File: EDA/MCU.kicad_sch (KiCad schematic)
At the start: 1 part, among them U7 STM32N657L0H3Q

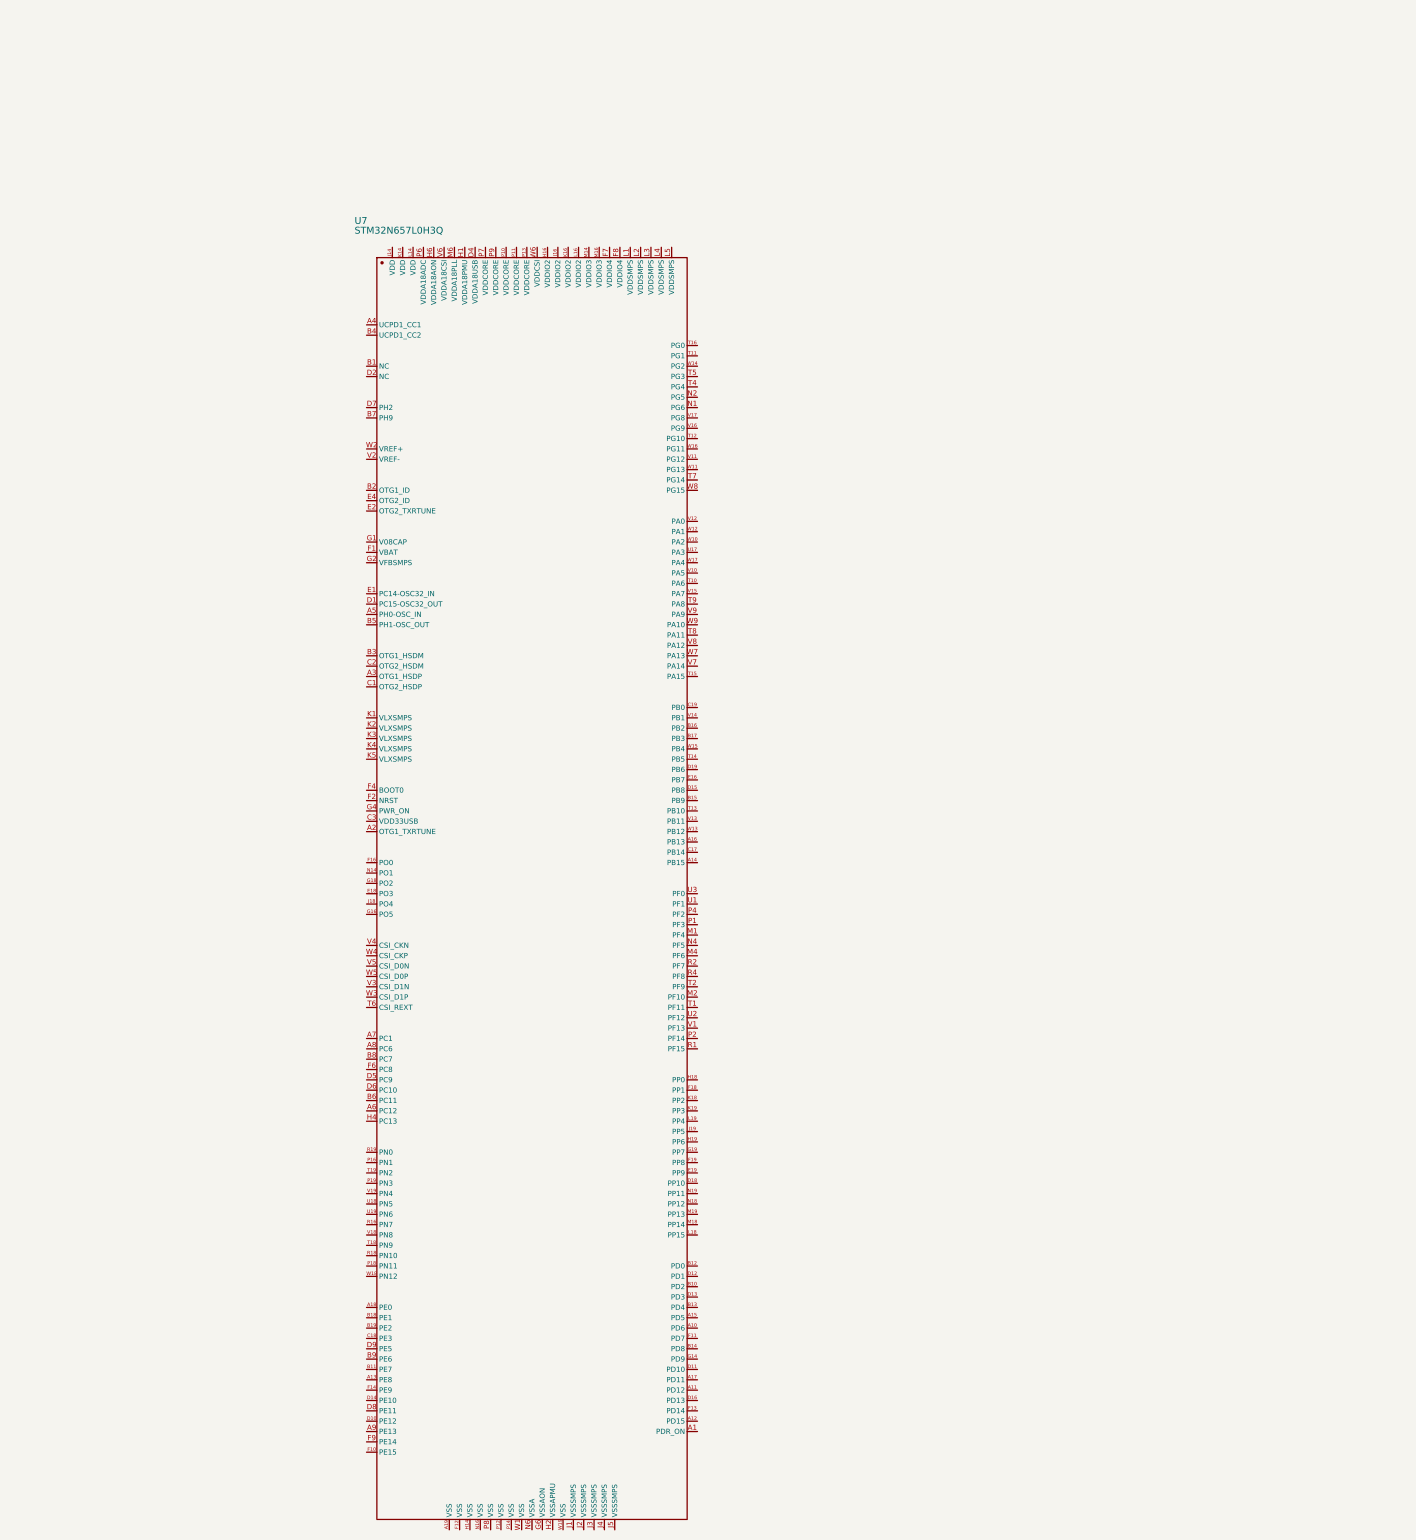
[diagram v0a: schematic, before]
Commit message: Changed STM32 MCU type, and added SDRAM. Micro-SD card slot has also been set up.
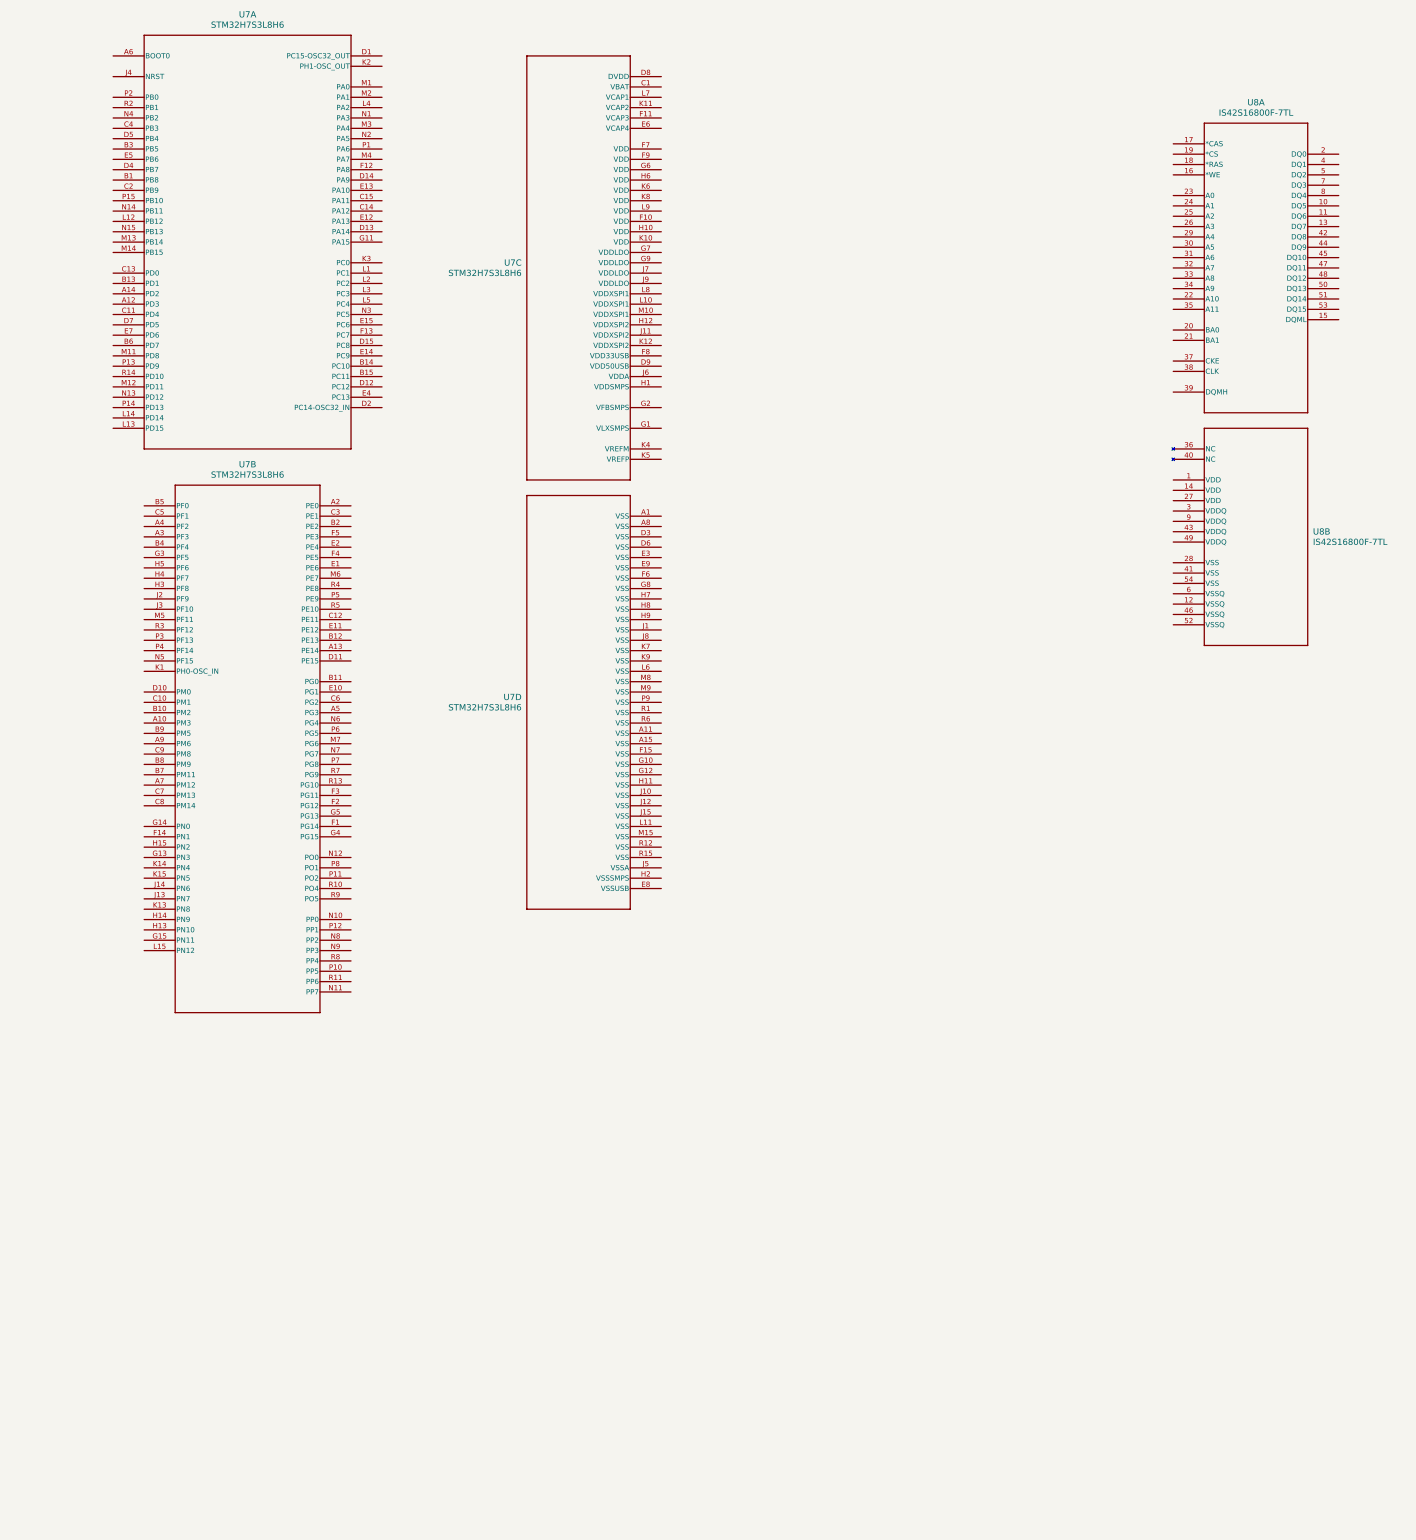
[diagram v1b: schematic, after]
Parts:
- removed U7: STM32N657L0H3Q, symbol STM32N657L0H3Q
- added U7: STM32H7S3L8H6, TFBGA225_13X13_STM, symbol CANSAT-lib:STM32H7S3L8H6
- added U8: IS42S16800F-7TL, CANSAT-lib:TSOP-II-54_ISI, symbol CANSAT-lib:IS42S16800F-7TL

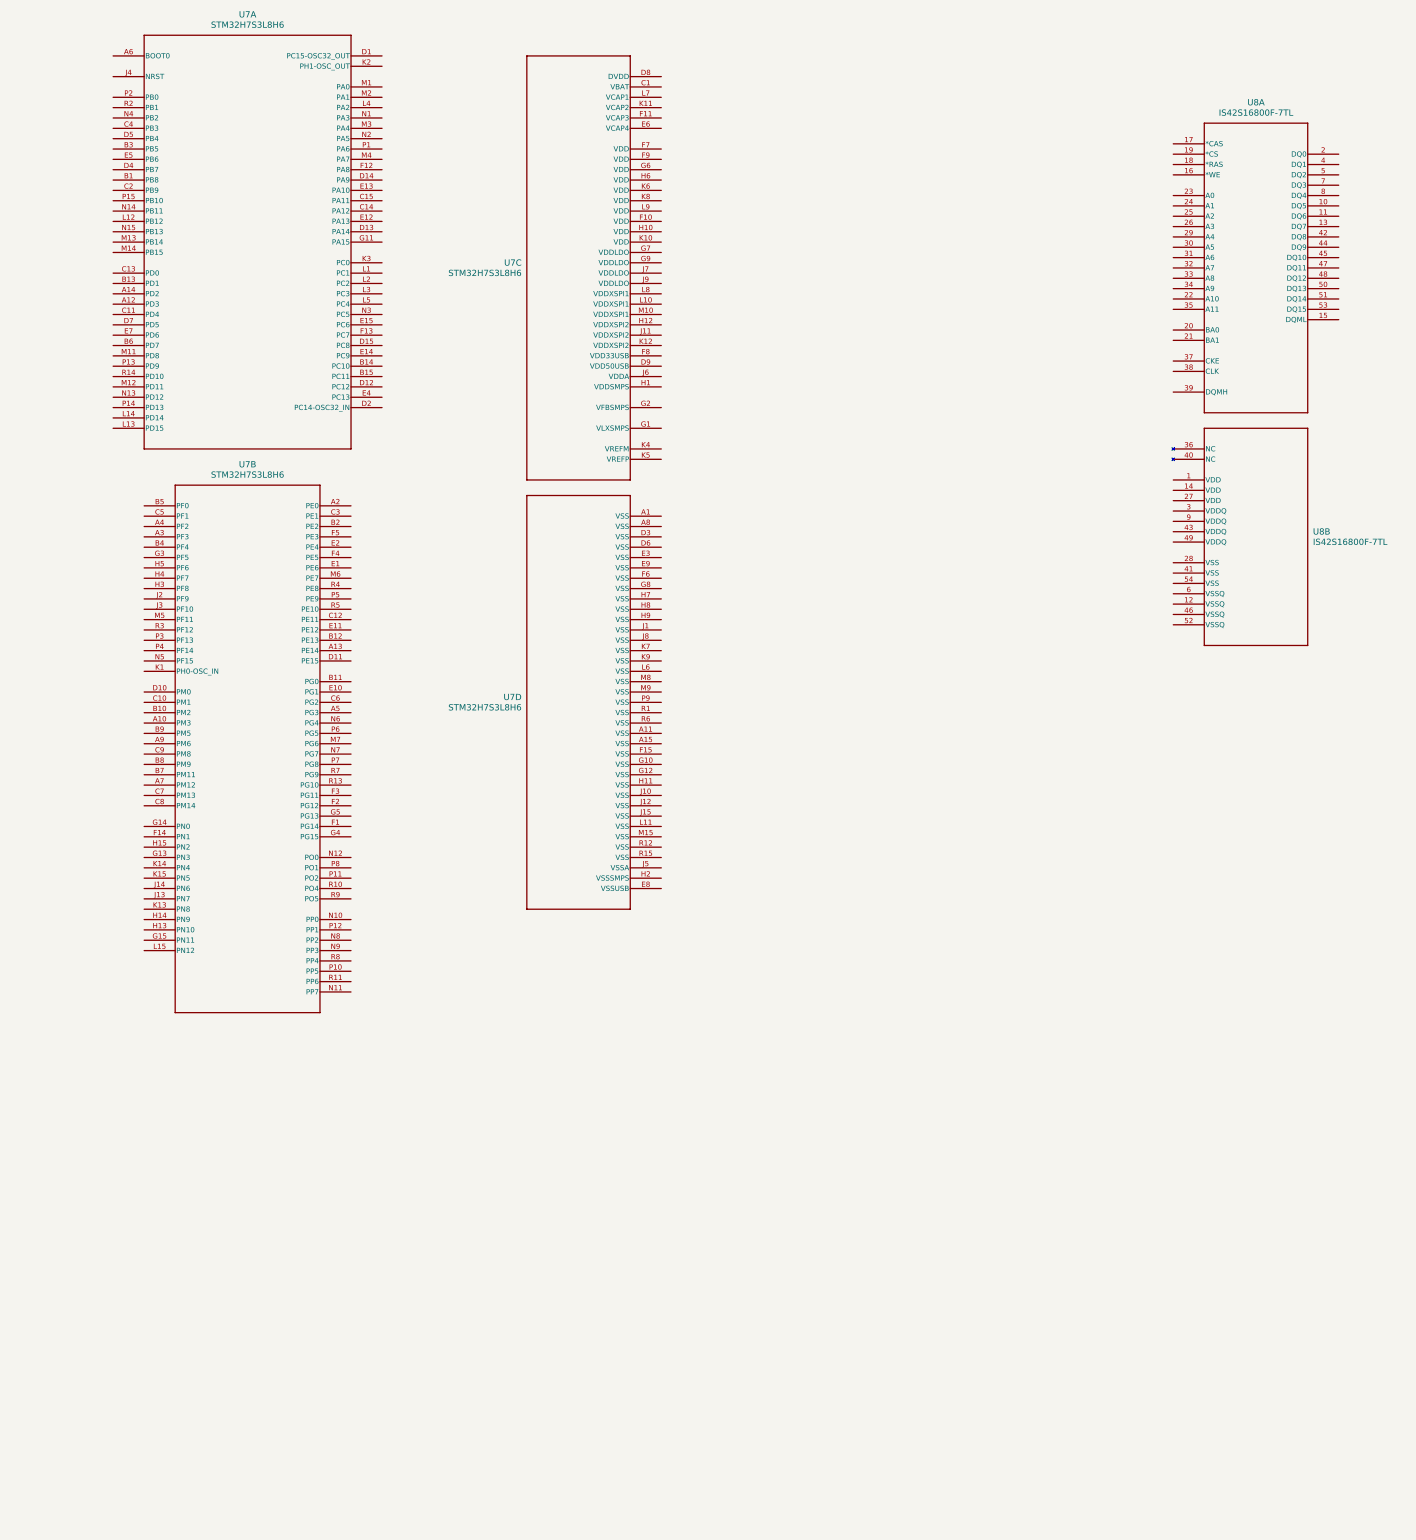
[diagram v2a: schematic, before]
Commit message: Did some scheamtic restruscturing as well as hooked up SDRAM and Micro-SD to STM32 core. Additional low power STM32 has also been added to power control. Firmware .IOC files have also been added for both STM32's
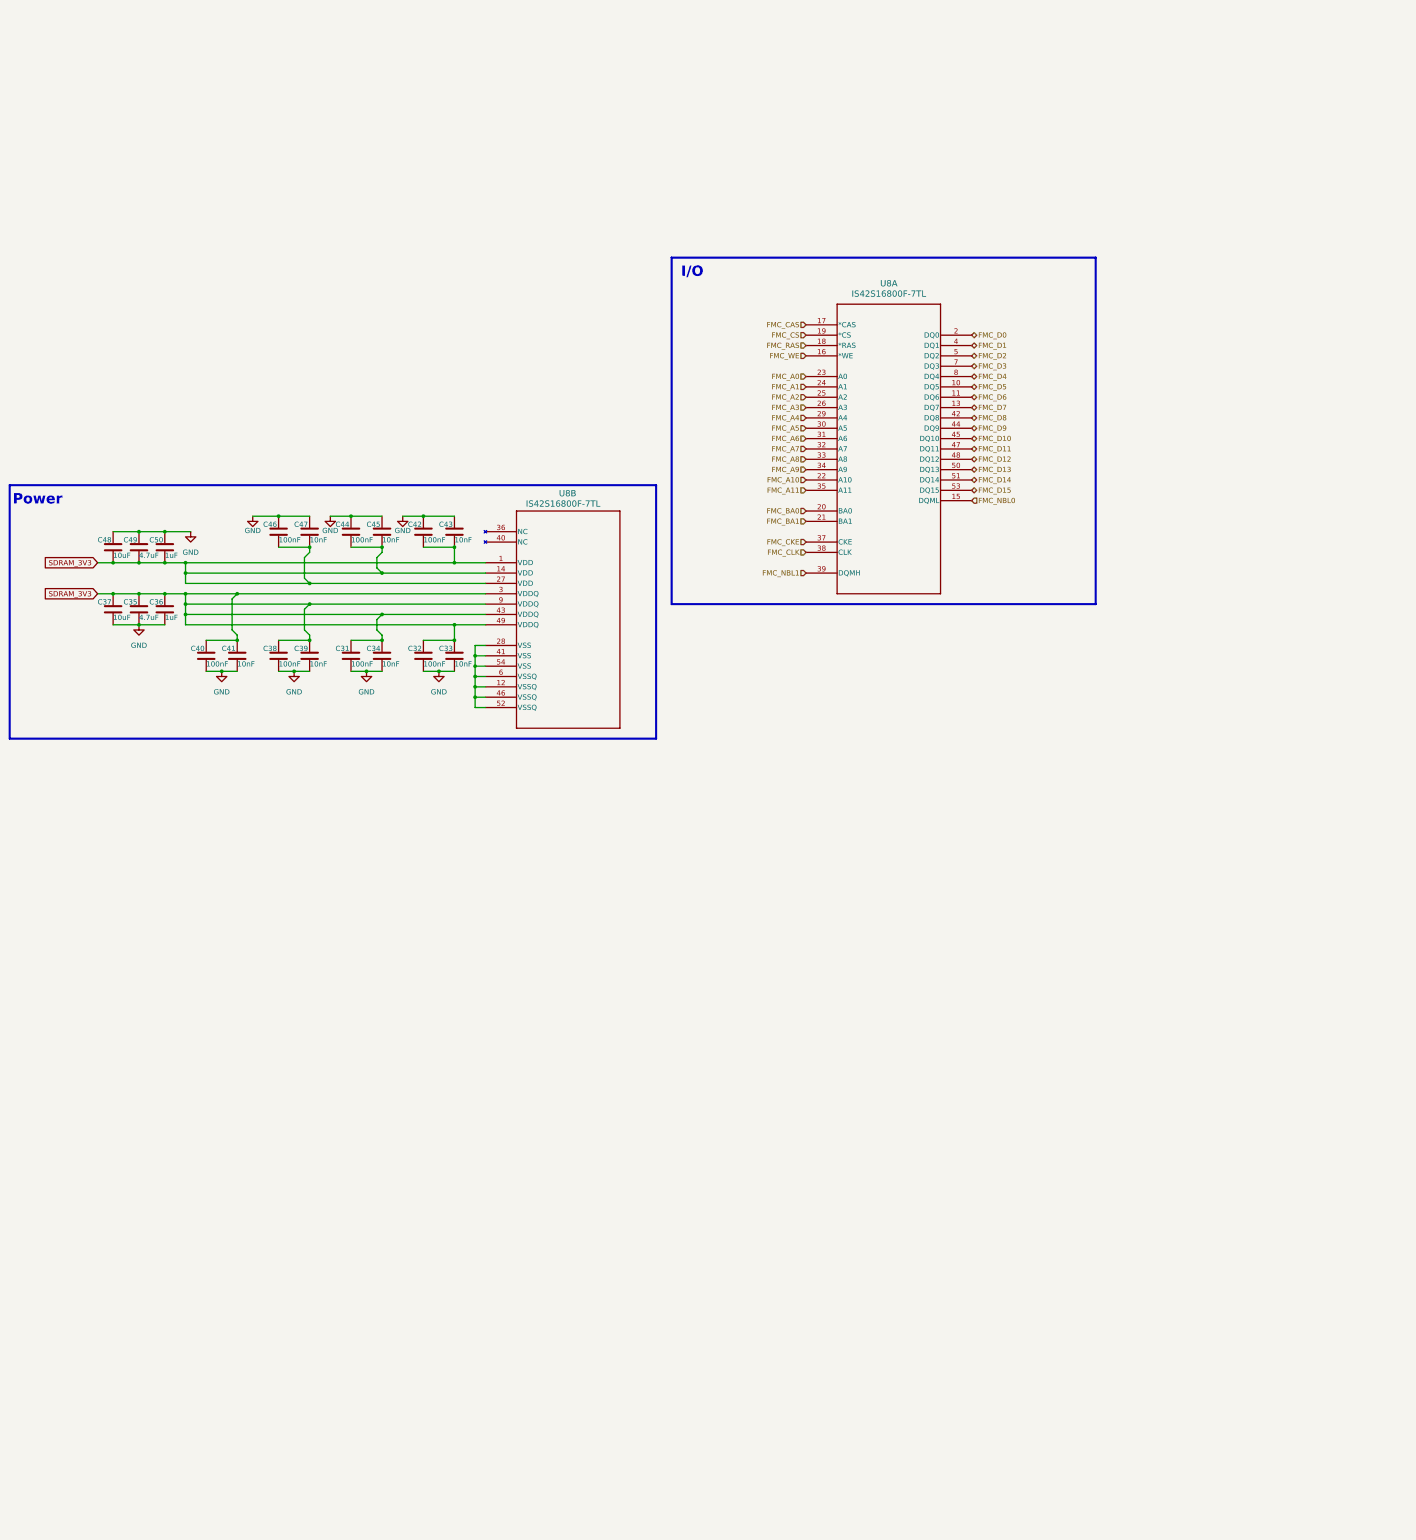
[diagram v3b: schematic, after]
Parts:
- removed U7: STM32H7S3L8H6, TFBGA225_13X13_STM, symbol CANSAT-lib:STM32H7S3L8H6
- added C31, C32, C38, C40, C42, C44, C46: 100nF, symbol Device:C
- added C33, C34, C39, C41, C43, C45, C47: 10nF, symbol Device:C
- added C35, C49: 4.7uF, symbol Device:C
- added C36, C50: 1uF, symbol Device:C
- added C37, C48: 10uF, symbol Device:C
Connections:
- net SDRAM_3V3: now reaches U8.1 (VDD)
- net SDRAM_3V3: now also U8.14 (VDD), U8.27 (VDD), U8.3 (VDDQ), U8.43 (VDDQ), U8.49 (VDDQ), U8.9 (VDDQ), C31.1, C32.1, C33.1, C34.1, C35.1, C36.1, C37.1, C38.1, C39.1, C40.1, C41.1, C42.2, C43.2, C44.2, C45.2, C46.2, C47.2, C48.2, C49.2, C50.2
- net at U8.12 (VSSQ): now also U8.28 (VSS), U8.41 (VSS), U8.46 (VSSQ), U8.52 (VSSQ), U8.54 (VSS), U8.6 (VSSQ)
- net FMC_D5: now reaches U8.10 (DQ5)
- net FMC_D6: now reaches U8.11 (DQ6)
- net FMC_D7: now reaches U8.13 (DQ7)
- net FMC_NBL0: now reaches U8.15 (DQML)
- net FMC_WE: now reaches U8.16 (*WE)
- net FMC_CAS: now reaches U8.17 (*CAS)
- net FMC_RAS: now reaches U8.18 (*RAS)
- net FMC_CS: now reaches U8.19 (*CS)
- net FMC_D0: now reaches U8.2 (DQ0)
- net FMC_BA0: now reaches U8.20 (BA0)
- net FMC_BA1: now reaches U8.21 (BA1)
- net FMC_A10: now reaches U8.22 (A10)
- net FMC_A0: now reaches U8.23 (A0)
- net FMC_A1: now reaches U8.24 (A1)
- net FMC_A2: now reaches U8.25 (A2)
- net FMC_A3: now reaches U8.26 (A3)
- net FMC_A4: now reaches U8.29 (A4)
- net FMC_A5: now reaches U8.30 (A5)
- net FMC_A6: now reaches U8.31 (A6)
- net FMC_A7: now reaches U8.32 (A7)
- net FMC_A8: now reaches U8.33 (A8)
- net FMC_A9: now reaches U8.34 (A9)
- net FMC_A11: now reaches U8.35 (A11)
- net FMC_CKE: now reaches U8.37 (CKE)
- net FMC_CLK: now reaches U8.38 (CLK)
- net FMC_NBL1: now reaches U8.39 (DQMH)
- net FMC_D1: now reaches U8.4 (DQ1)
- net FMC_D8: now reaches U8.42 (DQ8)
- net FMC_D9: now reaches U8.44 (DQ9)
- net FMC_D10: now reaches U8.45 (DQ10)
- net FMC_D11: now reaches U8.47 (DQ11)
- net FMC_D12: now reaches U8.48 (DQ12)
- net FMC_D2: now reaches U8.5 (DQ2)
- net FMC_D13: now reaches U8.50 (DQ13)
- net FMC_D14: now reaches U8.51 (DQ14)
- net FMC_D15: now reaches U8.53 (DQ15)
- net FMC_D3: now reaches U8.7 (DQ3)
- net FMC_D4: now reaches U8.8 (DQ4)
- new net GND: C31.2, C32.2, C33.2, C34.2, C35.2, C36.2, C37.2, C38.2, C39.2, C40.2, C41.2, C42.1, C43.1, C44.1, C45.1, C46.1, C47.1, C48.1, C49.1, C50.1
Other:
- note added: "I/O"
- note added: "Power"
- moved on the sheet: U8A, U8B
